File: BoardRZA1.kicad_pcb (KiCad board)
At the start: 4 copper layers, 99.9 x 80 mm, 172 parts, among them CON1 USB-MINI-B, CON2 USB-A-PCB, CON3 microSD, CON4 BARREL_JACK, J1 HR911105A, J2 SIL38, P1 CONN_5X2, SW1 RESET, SW2 NMI, SW3 SW0, SW4 SW1, U1 RZ-A1L, U2 13MHz, U3 48MHz, U4 N25QXXX, U5 AS4C16M16S, U6 BA3259HFP, U7 BU42xx, U8 KSZ8041MLL, U9 25MHz, X1 32.768k

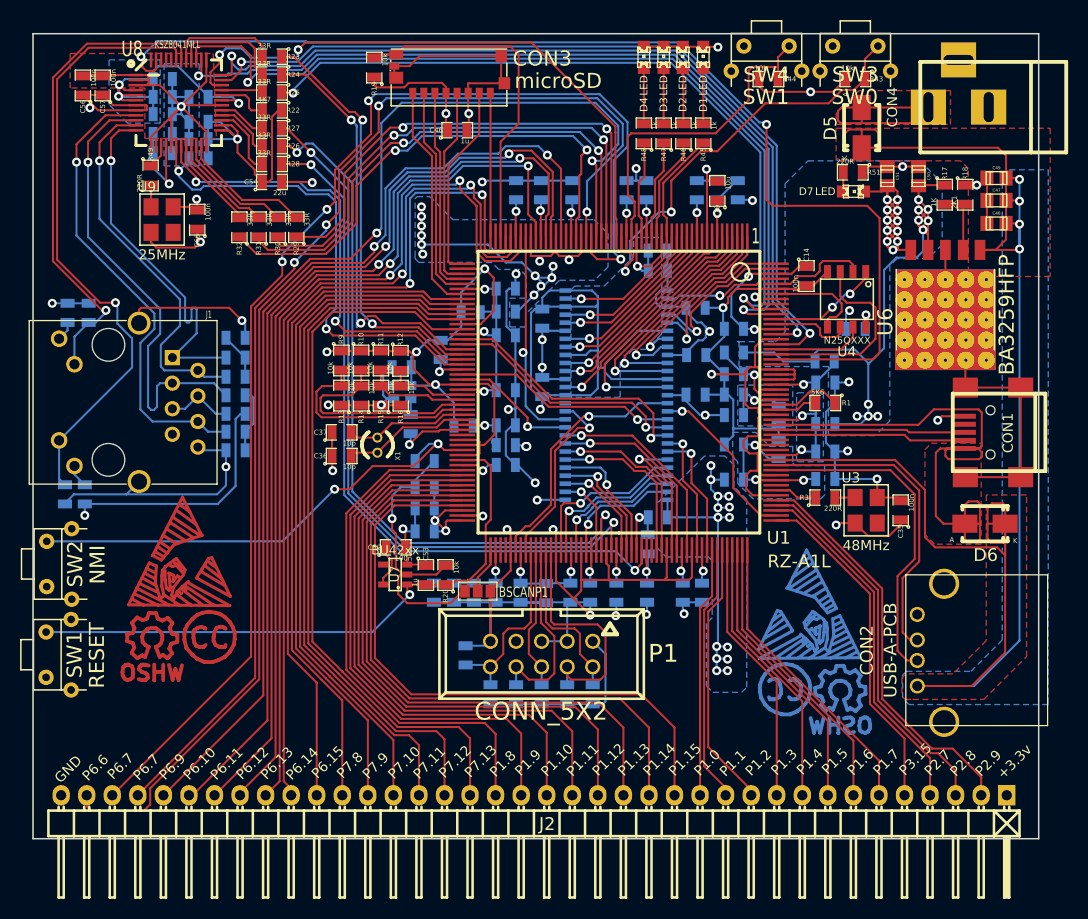
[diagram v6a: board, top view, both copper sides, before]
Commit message: Add vias to decouple cap. over VSS.
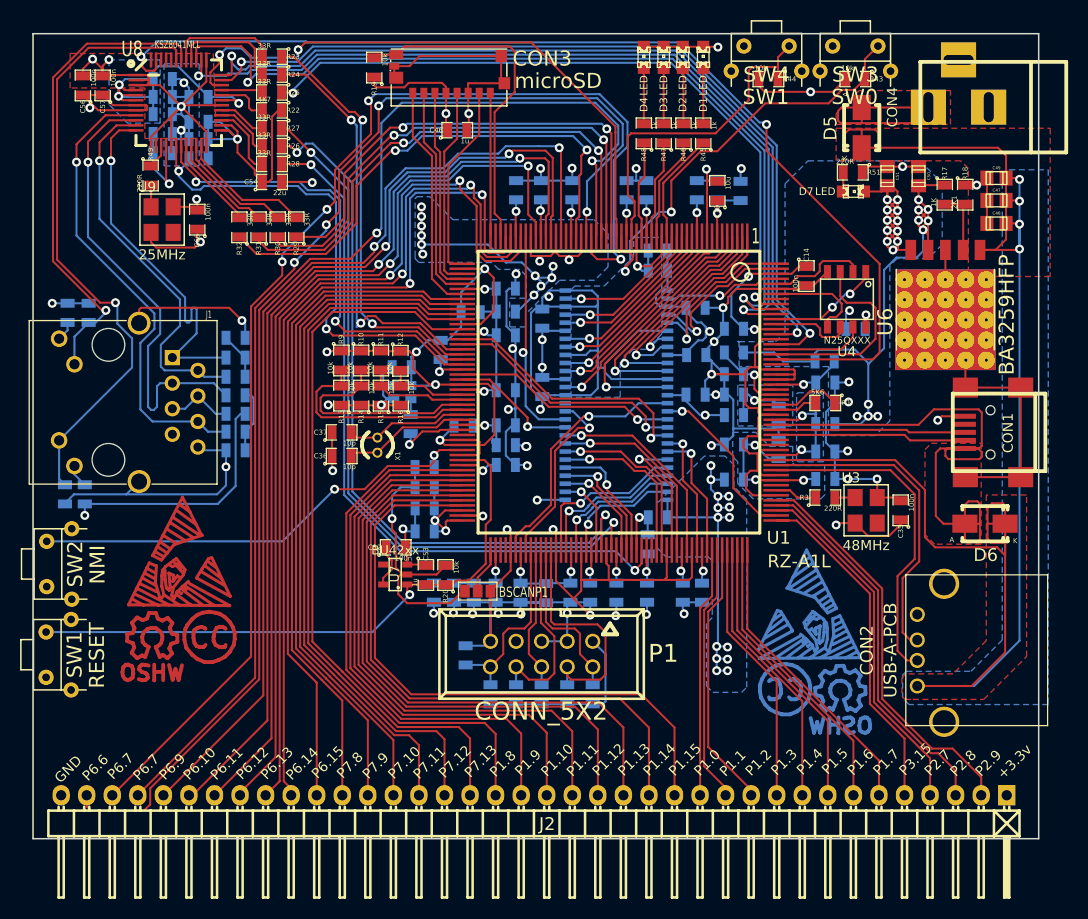
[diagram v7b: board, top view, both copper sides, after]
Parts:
- moved R42 0.60 mm to (58.8, 60.7), turned to 180 degrees
- moved L5 0.29 mm to (90.2, 33.2), turned to 90 degrees
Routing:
- net VSS: track 601.8 -> 625.2 mm, vias 40 -> 59
- net /PHY_RESET: track 113.2 -> 107.7 mm
- net /NMI: track 48.7 -> 46.6 mm
- net /P6_9: track 99.3 -> 100.4 mm
- net /P6_10: track 96.8 -> 97.6 mm
- net /P6_11: track 94.5 -> 95.2 mm
- net +3.3V: track 323.4 -> 322.7 mm

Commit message: Add testpoints
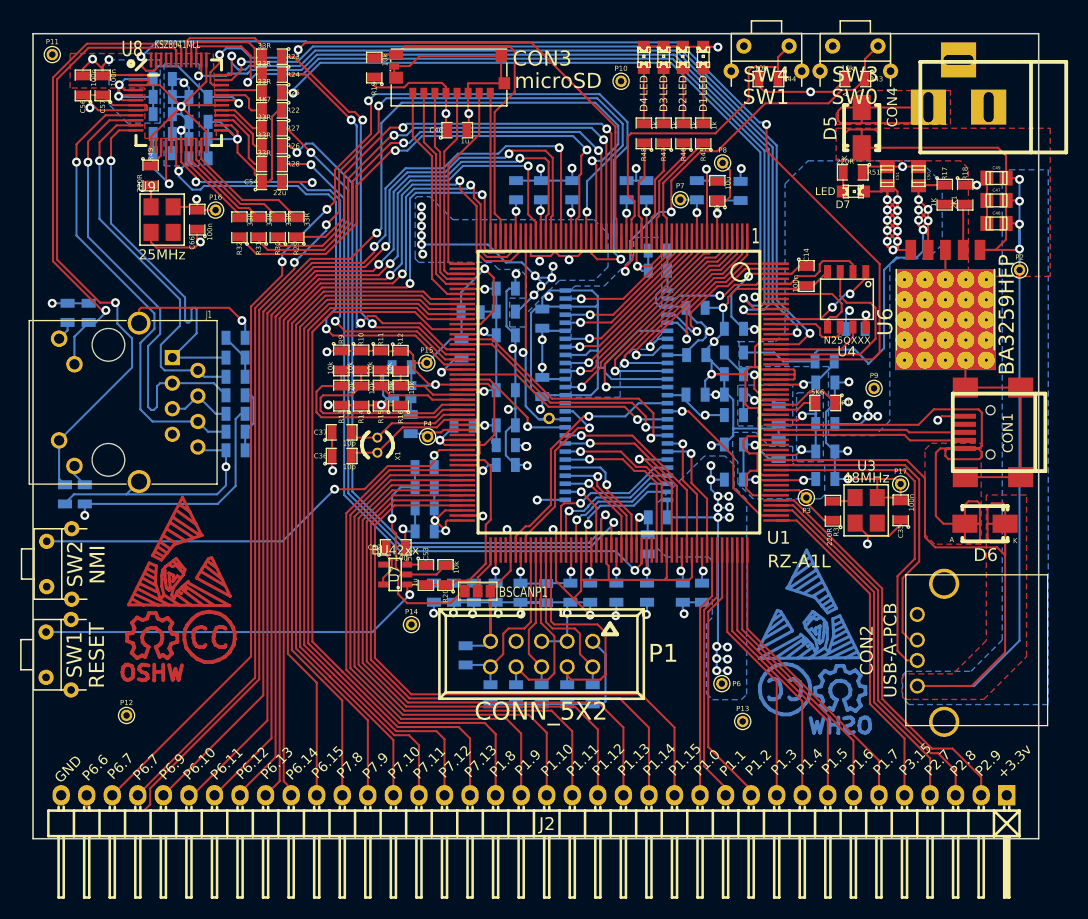
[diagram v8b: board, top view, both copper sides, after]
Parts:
- added P10: CONN_1, Connect:PINTST, F.Cu at (78.3, 22.3)
- added P11: CONN_1, Connect:PINTST, F.Cu at (21.8, 19.7)
- added P12: CONN_1, Connect:PINTST, F.Cu at (29.2, 85.3)
- added P13: CONN_1, Connect:PINTST, F.Cu at (90.4, 85.9)
- added P14: CONN_1, Connect:PINTST, F.Cu at (57.5, 76.3)
- added P15: CONN_1, Connect:PINTST, F.Cu at (59.0, 50.3)
- added P16: CONN_1, Connect:PINTST, F.Cu at (38.0, 35.1)
- added P17: CONN_1, Connect:PINTST, F.Cu at (106.1, 62.3)
- added P2: CONN_1, Connect:PINTST, F.Cu at (117.9, 41.1)
- added P3: CONN_1, Connect:PINTST, F.Cu at (96.7, 63.7)
- added P4: CONN_1, Connect:PINTST, F.Cu at (59.1, 57.6)
- added P5: CONN_1, Connect:PINTST, B.Cu at (71.2, 55.8)
- added P6: CONN_1, Connect:PINTST, F.Cu at (88.3, 82.2)
- added P7: CONN_1, Connect:PINTST, F.Cu at (84.2, 34.1)
- added P8: CONN_1, Connect:PINTST, F.Cu at (88.4, 30.4)
- added P9: CONN_1, Connect:PINTST, F.Cu at (103.5, 52.8)
- moved C17 2.07 mm to (62.5, 48.9)
- moved R3 1.52 mm to (99.4, 65.0), turned to 90 degrees
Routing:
- net /VCC: track 130.5 -> 62.9 mm
- net VSS: track 625.2 -> 632.3 mm, vias 59 -> 57
- net +1.2V: track 66.6 -> 62.6 mm
- net /USB_CLK: track 4.24 -> 7.17 mm
- net /PVCC: track 182.8 -> 184.5 mm
- net Net-(P4-Pad1): track 6.99 -> 5.53 mm, vias 1 -> 0
- net +3.3V: track 322.7 -> 321.6 mm
- net /RAM_CLK: track 21.6 -> 22.5 mm
- net Net-(CON2-Pad2): track 33.4 -> 34.2 mm
- net /+5v: track 169.0 -> 169.7 mm
- net Net-(CON2-Pad3): track 31.8 -> 32.5 mm
